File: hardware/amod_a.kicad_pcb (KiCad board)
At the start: 4 copper layers, 100 x 100 mm, 114 parts, among them J101 USB-C, J102 rails, J1101 SMA, J1102 TX, J1103 RX, J1104 Pmod, J201 SMA, J202 SMA, J301 SMA, J302 SMA, J401 SMA, J402 SMA, J501 SMA, J502 R, J601 SMA, J801 SMA, Q1101 AO3401A, Q201 AO3401A, Q301 AO3401A, Q401 AO3401A, Q501 AO3401A, Q601 AO3401A, Q801 AO3401A, Q802 AO3400A, SW1101 ON, SW201 ON, SW301 ON, SW401 ON, SW501 ON, SW502 DIP2, SW601 ON, SW801 ON, U101 LM2664, U102 3.3V, U1101 DRV8837, U1102 OPA810, U201 OPA810, U301 OPA810, U401 OPA847, U501 LT6230, U601 TLV3501, U801 TMP235

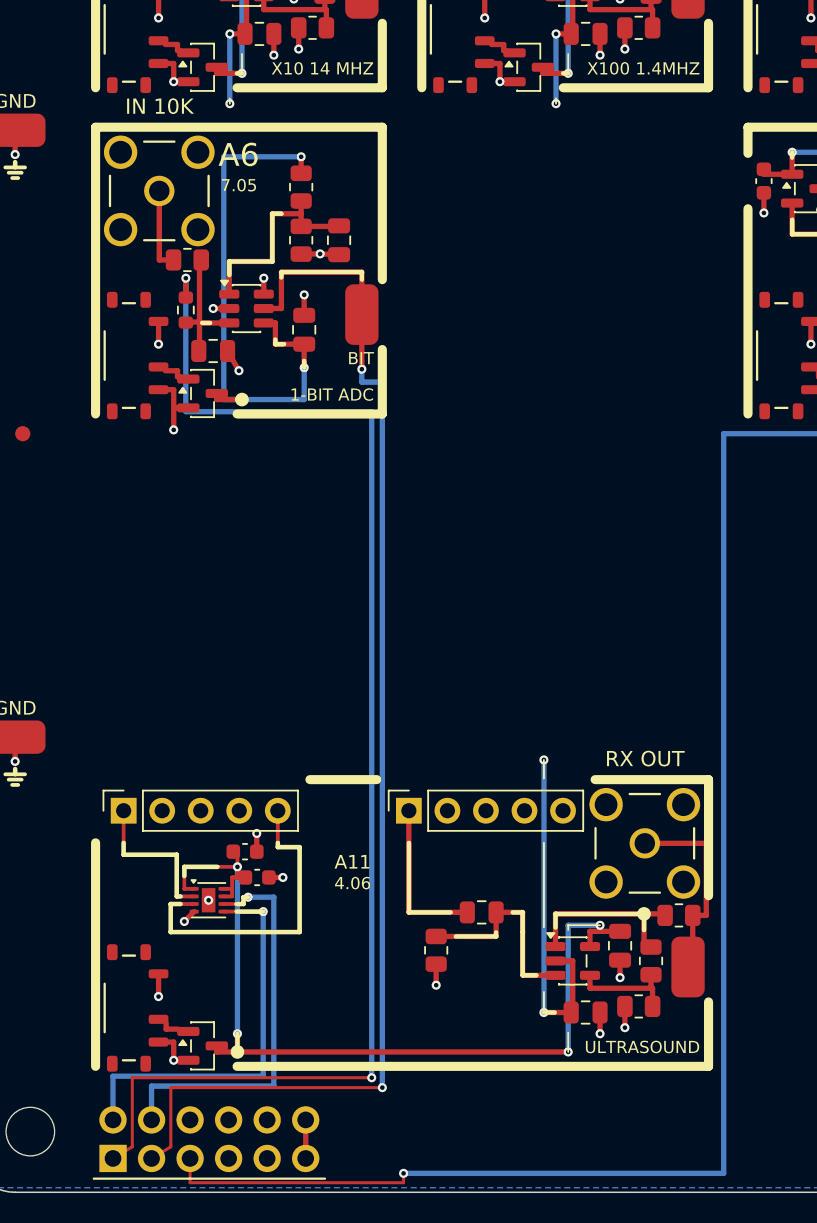
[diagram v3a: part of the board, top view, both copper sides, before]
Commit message: AMOD-A A7 (4046 PLL) and A9 (MC1496 mixer) at DRC 0; the Pmod corridor moved left of A9's LO jack; 0402 passives
Co-Authored-By: Claude Fable 5.1 <noreply@anthropic.com>
Claude-Session: https://claude.ai/code/session_01RKeoKvFFzjk3cEBLCXXHnB
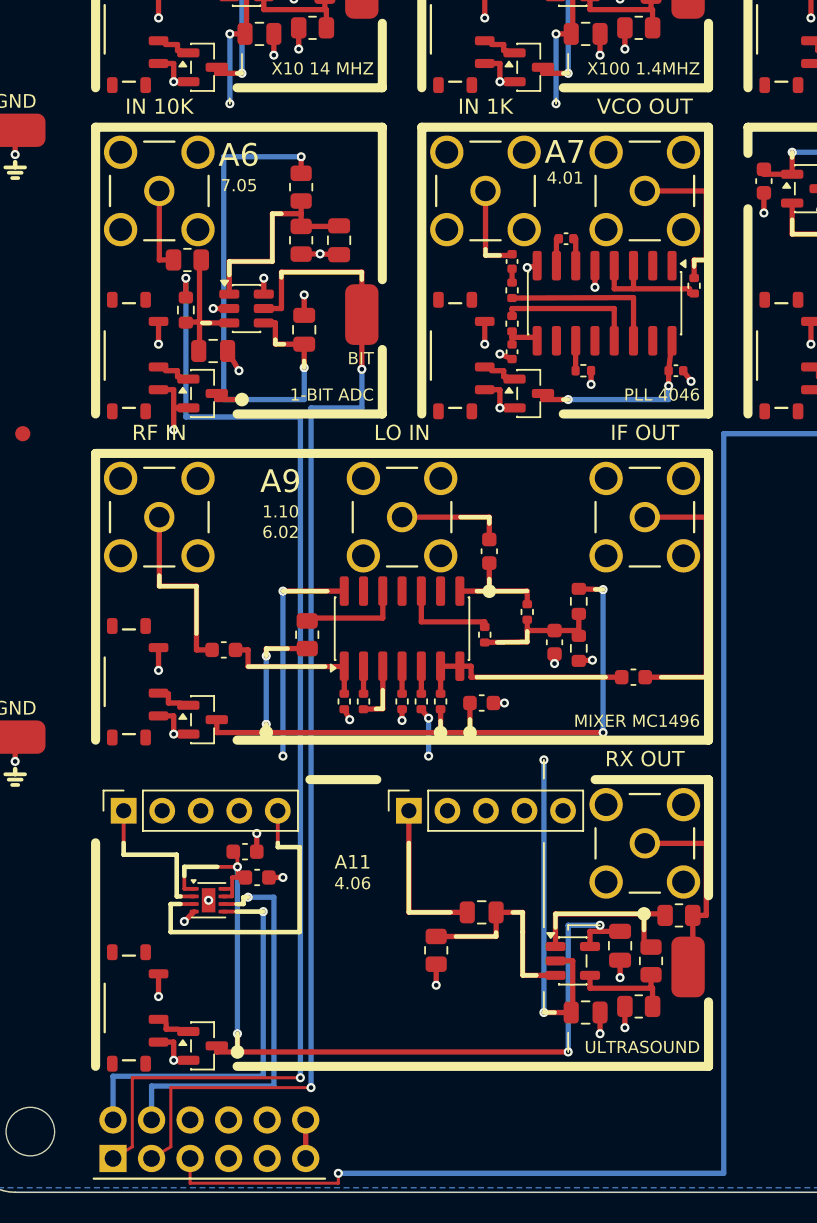
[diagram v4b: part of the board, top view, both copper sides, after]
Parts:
- added C701: 100n, Capacitor_SMD:C_0402_1005Metric, F.Cu at (35.8, 38.6)
- added C702: 100n, Capacitor_SMD:C_0402_1005Metric, F.Cu at (35.8, 44.6)
- added C703: 1n, Capacitor_SMD:C_0402_1005Metric, F.Cu at (39.3, 37.1)
- added C704: 100n, Capacitor_SMD:C_0402_1005Metric, F.Cu at (46.5, 45.9)
- added C901: 100n, Capacitor_SMD:C_0603_1608Metric, F.Cu at (16.8, 64.2)
- added C902: 100n, Capacitor_SMD:C_0603_1608Metric, F.Cu at (34.2, 57.8)
- added C903: 100n, Capacitor_SMD:C_0603_1608Metric, F.Cu at (38.5, 63.8)
- added C904: 100n, Capacitor_SMD:C_0603_1608Metric, F.Cu at (33.8, 67.8)
- added C905: 100n, Capacitor_SMD:C_0603_1608Metric, F.Cu at (43.8, 66.0)
- added J701: SMA, amod:SMA_BWSMA-KE-Z001_Vertical, F.Cu at (34.0, 34.0)
- added J702: SMA, amod:SMA_BWSMA-KE-Z001_Vertical, F.Cu at (44.5, 34.0)
- added J901: SMA, amod:SMA_BWSMA-KE-Z001_Vertical, F.Cu at (12.5, 55.5)
- added J902: SMA, amod:SMA_BWSMA-KE-Z001_Vertical, F.Cu at (28.5, 55.5)
- added J903: SMA, amod:SMA_BWSMA-KE-Z001_Vertical, F.Cu at (44.5, 55.5)
- added Q701: AO3401A, Package_TO_SOT_SMD:SOT-23, F.Cu at (36.9, 47.4)
- added Q901: AO3401A, Package_TO_SOT_SMD:SOT-23, F.Cu at (15.3, 68.8)
- added R701: 1k, Resistor_SMD:R_0402_1005Metric, F.Cu at (35.8, 40.5)
- added R702: 10k, Resistor_SMD:R_0402_1005Metric, F.Cu at (35.8, 42.8)
- added R703: 10k, Resistor_SMD:R_0402_1005Metric, F.Cu at (40.5, 45.9)
- added R704: 470, Resistor_SMD:R_0402_1005Metric, F.Cu at (47.8, 40.2)
- added R901: 51, Resistor_SMD:R_0402_1005Metric, F.Cu at (24.7, 67.7)
- added R902: 1k, Resistor_SMD:R_0402_1005Metric, F.Cu at (26.0, 67.7)
- added R903: 51, Resistor_SMD:R_0402_1005Metric, F.Cu at (28.5, 67.7)
- added R904: 3.9k, Resistor_SMD:R_0402_1005Metric, F.Cu at (29.8, 67.7)
- added R905: 1.5k, Resistor_SMD:R_0402_1005Metric, F.Cu at (31.0, 67.7)
- added R906: 1.5k, Resistor_SMD:R_0805_2012Metric, F.Cu at (22.2, 63.2)
- added R907: 51, Resistor_SMD:R_0402_1005Metric, F.Cu at (34.0, 63.2)
- added R908: 51, Resistor_SMD:R_0402_1005Metric, F.Cu at (36.8, 61.8)
- added R909: 10k, Resistor_SMD:R_0603_1608Metric, F.Cu at (40.1, 61.0)
- added R910: 10k, Resistor_SMD:R_0603_1608Metric, F.Cu at (40.1, 64.2)
- added SW701: ON, amod:SW_SPDT_Shouhan_MSK12C02, F.Cu at (32.0, 44.9)
- added SW901: ON, amod:SW_SPDT_Shouhan_MSK12C02, F.Cu at (10.5, 66.3)
- added U701: HC4046, Package_SO:SOIC-16_3.9x9.9mm_P1.27mm, F.Cu at (41.9, 41.4)
- added U901: MC1496, Package_SO:SOIC-14_3.9x8.7mm_P1.27mm, F.Cu at (28.5, 62.9)
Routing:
- net /A9_VS: track 0.00 -> 49.1 mm, vias 0 -> 4
- net /A9_IF: track 0.00 -> 18.6 mm
- net -5V: track 86.2 -> 104.4 mm, vias 14 -> 18
- net /A9_OUTA: track 0.00 -> 14.5 mm
- net /A7_VS: track 0.00 -> 12.6 mm, vias 0 -> 2
- net /A9_RF: track 0.00 -> 12.2 mm
- net GND: track 76.9 -> 88.4 mm, vias 57 -> 69
- net /A7_SIG: track 0.00 -> 10.9 mm
- net /A7_OUT: track 0.00 -> 10.6 mm
- net /A9_SIGA: track 0.00 -> 10.1 mm
- net /A9_CB: track 0.00 -> 9.47 mm
- net /PMOD1: track 88.0 -> 78.6 mm
- net /A7_PC2: track 0.00 -> 9.35 mm
- net /A7_VCO_A: track 0.00 -> 8.63 mm
- net /A9_LO: track 0.00 -> 7.23 mm
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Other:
- board text added: "1.10"
- board text added: "4.01"
- board text added: "6.02"
- board text added: "A7"
- board text added: "A9"
- board text added: "IF OUT"
- board text added: "IN 1K"
- board text added: "LO IN"
- board text added: "MIXER MC1496"
- board text added: "PLL 4046"
- board text added: "RF IN"
- board text added: "VCO OUT"

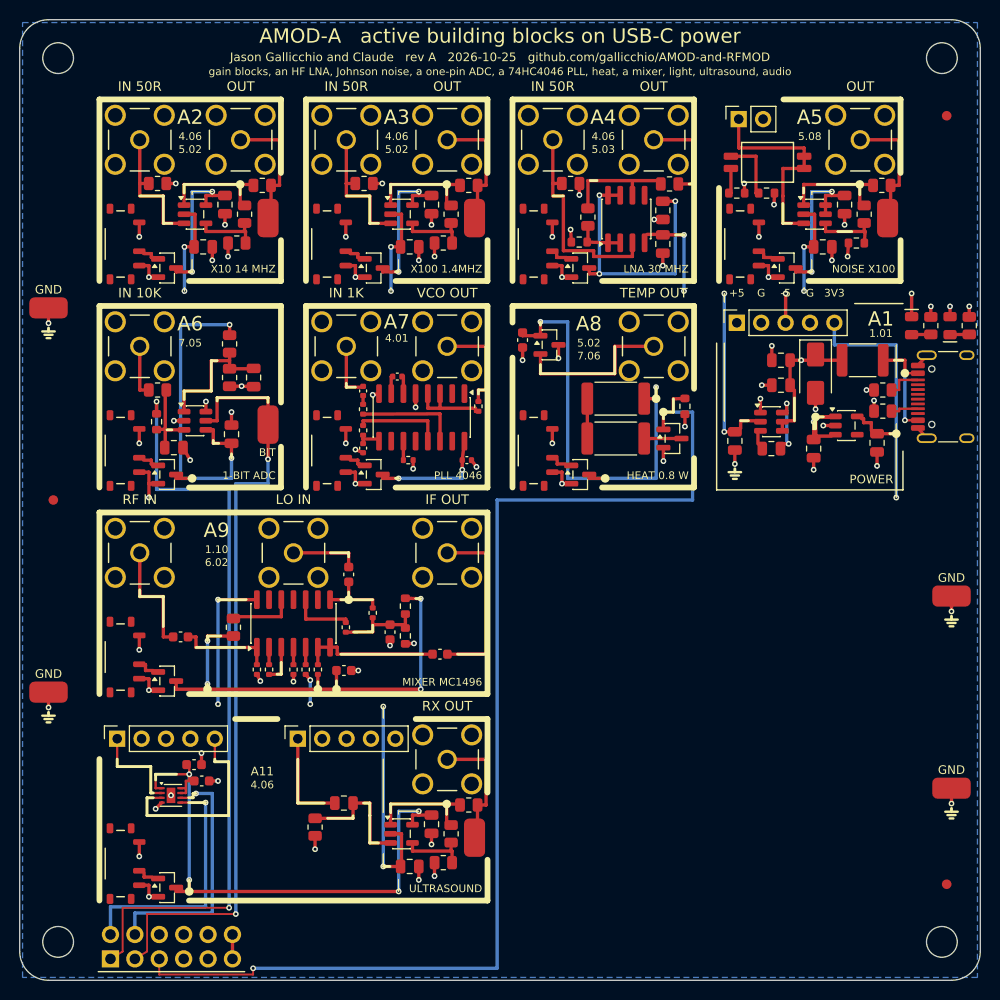
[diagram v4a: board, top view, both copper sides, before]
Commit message: AMOD-A complete: A10 (light) and A12 (audio) at DRC 0; all twelve tiles, the Pmod lines and the -5 V pour across both gutters
Co-Authored-By: Claude Fable 5.1 <noreply@anthropic.com>
Claude-Session: https://claude.ai/code/session_01RKeoKvFFzjk3cEBLCXXHnB
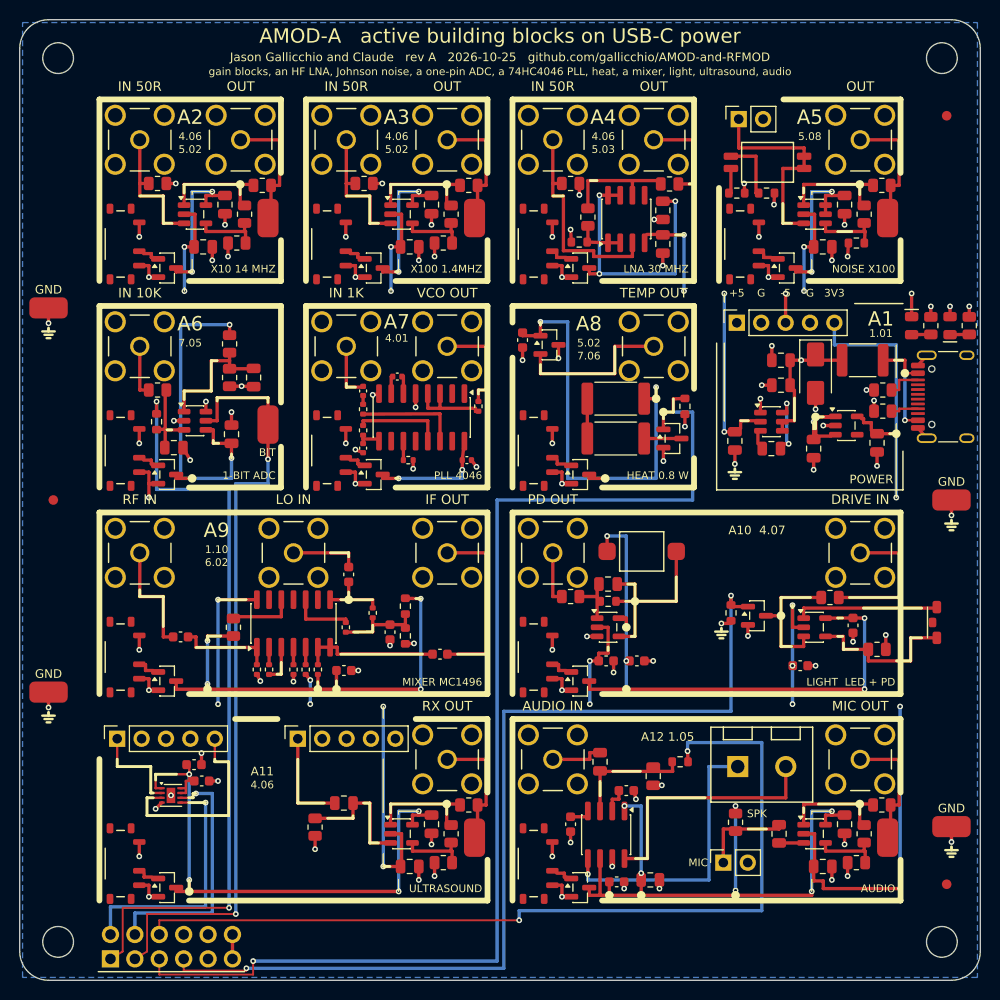
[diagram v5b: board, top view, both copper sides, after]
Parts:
- added C1001: 10p, Capacitor_SMD:C_0805_2012Metric, F.Cu at (61.2, 58.8)
- added C1002: 100n, Capacitor_SMD:C_0603_1608Metric, F.Cu at (61.0, 66.8)
- added C1003: 100n, Capacitor_SMD:C_0603_1608Metric, F.Cu at (64.2, 66.8)
- added C1004: 100n, Capacitor_SMD:C_0603_1608Metric, F.Cu at (81.2, 67.2)
- added C1005: 100n, Capacitor_SMD:C_0603_1608Metric, F.Cu at (86.8, 63.0)
- added C1201: 1u, Capacitor_SMD:C_0805_2012Metric, F.Cu at (60.4, 77.2)
- added C1202: 10n, Capacitor_SMD:C_0805_2012Metric, F.Cu at (66.0, 78.8)
- added C1203: 1u, Capacitor_SMD:C_0603_1608Metric, F.Cu at (57.4, 83.8)
- added C1204: 1u, Capacitor_SMD:C_0603_1608Metric, F.Cu at (63.1, 80.2)
- added C1205: 100n, Capacitor_SMD:C_0603_1608Metric, F.Cu at (62.1, 89.8)
- added C1206: 10u, Capacitor_SMD:C_0805_2012Metric, F.Cu at (65.7, 89.5)
- added C1207: 1u, Capacitor_SMD:C_0805_2012Metric, F.Cu at (79.0, 84.8)
- added C1208: 100n, Capacitor_SMD:C_0805_2012Metric, F.Cu at (85.9, 83.8)
- added C1209: 100n, Capacitor_SMD:C_0805_2012Metric, F.Cu at (83.6, 88.2)
- added D1001: PD70, amod:Photodiode_PD70-01C, F.Cu at (64.8, 55.4)
- added J1001: SMA, amod:SMA_BWSMA-KE-Z001_Vertical, F.Cu at (55.5, 55.5)
- added J1002: SMA, amod:SMA_BWSMA-KE-Z001_Vertical, F.Cu at (87.5, 55.5)
- added J1201: SMA, amod:SMA_BWSMA-KE-Z001_Vertical, F.Cu at (55.5, 77.0)
- added J1202: SMA, amod:SMA_BWSMA-KE-Z001_Vertical, F.Cu at (87.5, 77.0)
- added J1203: SPK, amod:TerminalBlock_KF301_1x02_P5.00mm, F.Cu at (77.2, 77.8)
- added J1204: MIC, Connector_PinSocket_2.54mm:PinSocket_1x02_P2.54mm_Vertical, F.Cu at (73.2, 87.8)
- added LED1001: LED, amod:LED_SideView_3.2x1.0mm_E6C1204, F.Cu at (95.2, 62.8)
- added Q1001: AO3401A, Package_TO_SOT_SMD:SOT-23, F.Cu at (58.4, 68.8)
- added Q1002: 2N7002, Package_TO_SOT_SMD:SOT-23, F.Cu at (76.8, 62.0)
- added Q1201: AO3401A, Package_TO_SOT_SMD:SOT-23, F.Cu at (58.4, 90.3)
- added R1001: 10k, Resistor_SMD:R_0603_1608Metric, F.Cu at (61.2, 60.5)
- added R1002: 49.9, Resistor_SMD:R_0805_2012Metric, F.Cu at (57.4, 60.0)
- added R1003: 1k, Resistor_SMD:R_0805_2012Metric, F.Cu at (84.3, 60.1)
- added R1004: 10k, Resistor_SMD:R_0603_1608Metric, F.Cu at (74.0, 61.8)
- added R1005: 22, Resistor_SMD:R_0805_2012Metric, F.Cu at (89.2, 65.5)
- added R1201: 10k, Resistor_SMD:R_0603_1608Metric, F.Cu at (68.8, 77.2)
- added R1202: 2.2k, Resistor_SMD:R_0805_2012Metric, F.Cu at (74.5, 83.5)
- added R1203: 10k, Resistor_SMD:R_0805_2012Metric, F.Cu at (87.9, 84.8)
- added R1204: 100R, Resistor_SMD:R_0805_2012Metric, F.Cu at (87.1, 87.8)
- added R1205: 49.9, Resistor_SMD:R_0805_2012Metric, F.Cu at (89.8, 81.8)
- added SW1001: ON, amod:SW_SPDT_Shouhan_MSK12C02, F.Cu at (53.5, 66.3)
- added SW1201: ON, amod:SW_SPDT_Shouhan_MSK12C02, F.Cu at (53.5, 87.8)
- added TP1201: OUT, amod:TestPoint_Loop_RH-5019, F.Cu at (90.3, 85.2)
- added U1001: OPA810, Package_TO_SOT_SMD:SOT-23-5, F.Cu at (61.2, 63.2)
- added U1002: OPA810, Package_TO_SOT_SMD:SOT-23-5, F.Cu at (82.8, 63.2)
- added U1201: PAM8302A, Package_SO:SOIC-8_3.9x4.9mm_P1.27mm, F.Cu at (61.0, 84.8)
- added U1202: OPA810, Package_TO_SOT_SMD:SOT-23-5, F.Cu at (82.8, 84.8)
- moved TP9903 10.0 mm to (97.0, 50.0)
- moved TP9904 4.00 mm to (97.0, 84.0)
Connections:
- J1104 pad 6: unconnected-(J1104-Pin_6-Pad6) -> /PMOD7
- J1104 pad 7: unconnected-(J1104-Pin_7-Pad7) -> /PMOD4
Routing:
- net /PMOD4: track 0.00 -> 100.2 mm, vias 0 -> 2
- net /PMOD7: track 0.00 -> 92.4 mm, vias 0 -> 2
- net /A12_VS: track 0.00 -> 65.1 mm, vias 0 -> 6
- net /A10_VS: track 0.00 -> 62.6 mm, vias 0 -> 6
- net -5V: track 104.4 -> 164.1 mm, vias 18 -> 25
- net /A12_VOP: track 0.00 -> 29.6 mm, vias 0 -> 1
- net /A12_VOM: track 0.00 -> 26.4 mm
- net GND: track 88.4 -> 109.6 mm, vias 69 -> 88
- net /A10_FB: track 0.00 -> 20.4 mm
- net /A10_SENSE: track 0.00 -> 16.5 mm
- net /A10_DRV_O: track 0.00 -> 15.0 mm
- net /A10_DRV: track 0.00 -> 15.0 mm
- net /A10_INP: track 0.00 -> 14.3 mm
- net /A12_OUT: track 0.00 -> 13.4 mm
- net /A12_NODE: track 0.00 -> 12.7 mm
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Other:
- board text added: "A10 4.07"
- board text added: "A12 1.05"
- board text added: "AUDIO"
- board text added: "AUDIO IN"
- board text added: "DRIVE IN"
- board text added: "LIGHT LED + PD"
- board text added: "MIC"
- board text added: "MIC OUT"
- board text added: "PD OUT"
- board text added: "SPK"

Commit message: Pmod plugs: fix the mirrored pinout on AMOD-A and RF-MOD (JLCPCB's numbering of the PZ254R runs opposite to KiCad's): plug two columns left, nets renamed to the standard IO numbers, a fab check of every plug pad; mounting holes replaced by four marked rubber feet on both boards
Co-Authored-By: Claude Opus 5.5 <noreply@anthropic.com>
Claude-Session: https://claude.ai/code/session_01RKeoKvFFzjk3cEBLCXXHnB
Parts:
- removed MH1, MH2, MH3, MH4: MountingHole, MountingHole:MountingHole_3.2mm_M3
- moved J1104 5.08 mm to (10.7, 96.5)
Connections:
- J1104 pad 1: /PMOD1 -> /PMOD_VCC
- J1104 pad 10: GND -> /PMOD2
- J1104 pad 11: /PMOD_VCC -> /PMOD5
- J1104 pad 12: /PMOD_VCC -> unconnected-(J1104-Pin_12-Pad12)
- J1104 pad 2: /PMOD5 -> /PMOD_VCC
- J1104 pad 3: /PMOD2 -> GND
- J1104 pad 4: /PMOD6 -> GND
- J1104 pad 5: /PMOD3 -> /PMOD8
- J1104 pad 6: /PMOD7 -> /PMOD4
- J1104 pad 7: /PMOD4 -> /PMOD7
- J1104 pad 8: unconnected-(J1104-Pin_8-Pad8) -> /PMOD3
- J1104 pad 9: GND -> /PMOD6
- Q1002 pad 1: /PMOD4 -> /PMOD5
- Q802 pad 1: /PMOD3 -> /PMOD6
- R1004 pad 1: /PMOD4 -> /PMOD5
- R1201 pad 2: /PMOD7 -> /PMOD2
- R602 pad 1: /PMOD1 -> /PMOD8
- R803 pad 1: /PMOD3 -> /PMOD6
- TP601 pad 1: /PMOD2 -> /PMOD7
- U1101 pad 5: /PMOD5 -> /PMOD4
- U1101 pad 6: /PMOD6 -> /PMOD3
- U601 pad 5: /PMOD2 -> /PMOD7
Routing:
- net /PMOD6: track 26.5 -> 124.2 mm, vias 1 -> 2
- net /PMOD3: track 124.2 -> 26.5 mm, vias 2 -> 1
- net /PMOD8: track 0.00 -> 78.6 mm, vias 0 -> 2
- net /PMOD1: track 78.6 -> 0.00 mm, vias 2 -> 0
- net /PMOD4: track 100.2 -> 26.3 mm, vias 2 -> 1
- net /PMOD5: track 26.3 -> 100.2 mm, vias 1 -> 2
- net /PMOD7: track 92.4 -> 80.6 mm
- net /PMOD2: track 80.6 -> 92.4 mm
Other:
- board text added: "FOOT"
